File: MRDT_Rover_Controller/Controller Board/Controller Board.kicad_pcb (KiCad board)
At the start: 2 copper layers, 137.6 x 81.5 mm, 32 parts, among them Q1 S8050, SW1 EG1218

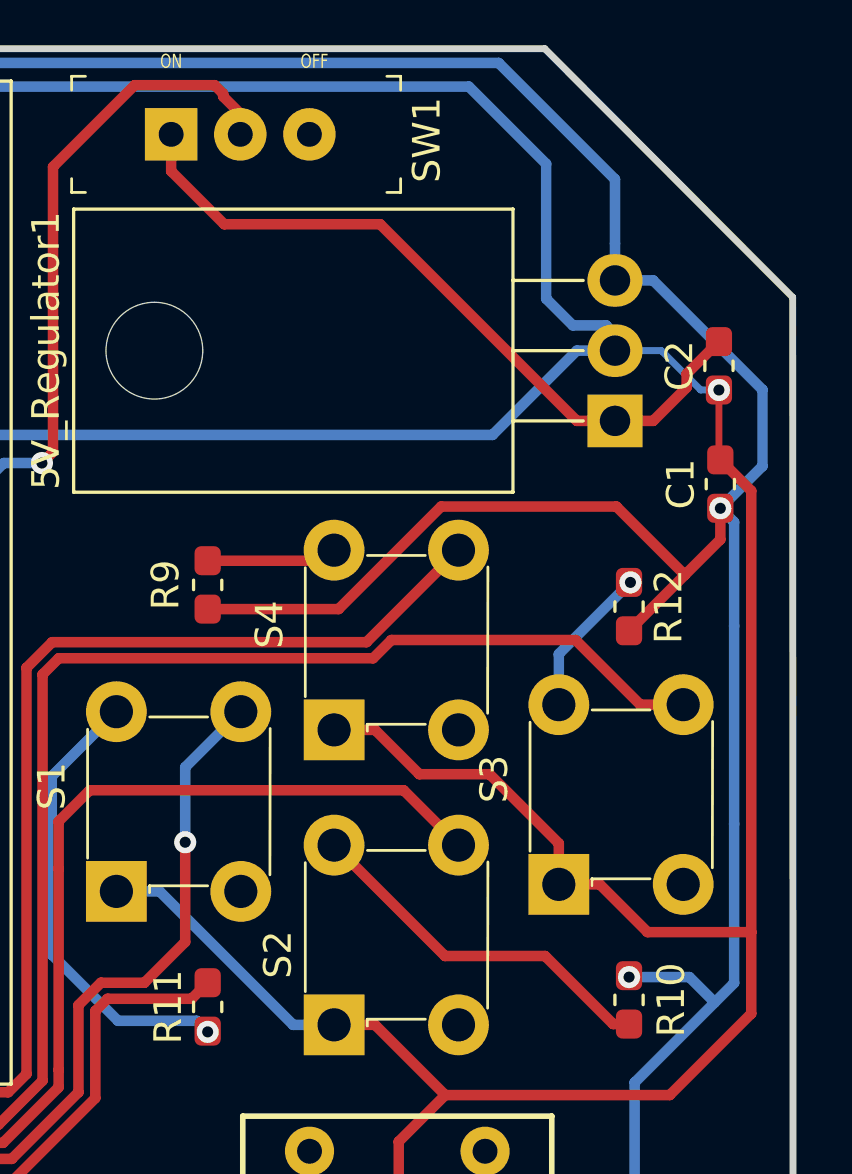
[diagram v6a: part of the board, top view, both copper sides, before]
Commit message: Trace corners re-adjusted
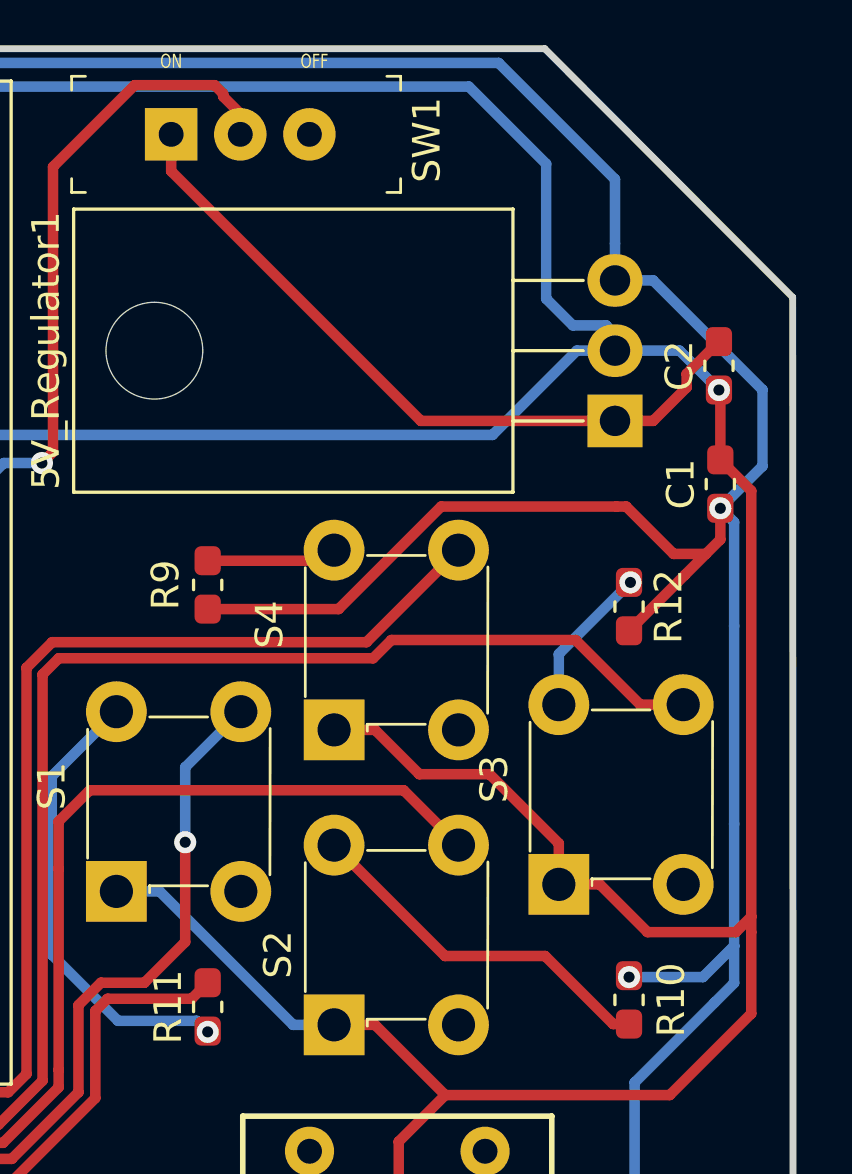
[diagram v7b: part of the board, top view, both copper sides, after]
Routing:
- net 5V: track 419.7 -> 421.0 mm
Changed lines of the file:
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@@
     (thickness 1.6)
     (drawings 30)
-    (tracks 651)
+    (tracks 655)
     (zones 0)
     (modules 32)
@@
   )
   (setup
-    (last_trace_width 0.25)
+    (last_trace_width 0.381)
     (user_trace_width 0.381)
     (user_trace_width 15)
@@
   (segment (start 92.71 96.278765) (end 86.995 90.563765) (width 0.381) (layer F.Cu) (net 14))
   (segment (start 92.71 97.536) (end 92.71 96.278765) (width 0.381) (layer F.Cu) (net 14))
-  (segment (start 210.82 64.4652) (end 210.7692 64.4144) (width 0.381) (layer F.Cu) (net 14))
   (segment (start 210.7692 66.8922) (end 210.82 66.943) (width 0.25) (layer F.Cu) (net 14))
-  (segment (start 210.7692 64.4144) (end 210.7692 66.8922) (width 0.25) (layer F.Cu) (net 14))
   (segment (start 210.7692 64.4144) (end 210.7692 64.4144) (width 0.381) (layer F.Cu) (net 14))
   (via (at 210.7692 64.4144) (size 0.8) (drill 0.4) (layers F.Cu B.Cu) (net 14))
-  (segment (start 210.7692 64.4144) (end 210.1088 64.4144) (width 0.25) (layer B.Cu) (net 14))
-  (segment (start 208.6864 62.992) (end 207.01 62.992) (width 0.25) (layer B.Cu) (net 14))
-  (segment (start 210.1088 64.4144) (end 208.6864 62.992) (width 0.25) (layer B.Cu) (net 14))
   (segment (start 189.527 82.55) (end 188.976 82.55) (width 0.381) (layer B.Cu) (net 14))
   (segment (start 200.871 89.916) (end 198.331 87.376) (width 0.381) (layer F.Cu) (net 14))
@@
   (segment (start 206.459 82.296) (end 204.978 82.296) (width 0.381) (layer F.Cu) (net 14))
   (segment (start 208.1862 84.0232) (end 206.459 82.296) (width 0.381) (layer F.Cu) (net 14))
-  (segment (start 211.9376 84.0232) (end 208.1862 84.0232) (width 0.381) (layer F.Cu) (net 14))
   (segment (start 211.9376 84.0232) (end 211.9376 86.9696) (width 0.381) (layer F.Cu) (net 14))
-  (segment (start 211.9376 68.0606) (end 211.9376 84.0232) (width 0.381) (layer F.Cu) (net 14))
   (segment (start 198.331 76.708) (end 196.85 76.708) (width 0.381) (layer F.Cu) (net 14))
   (segment (start 199.934391 78.311391) (end 198.331 76.708) (width 0.381) (layer F.Cu) (net 14))
@@
   (segment (start 196.85 87.376) (end 195.369 87.376) (width 0.381) (layer B.Cu) (net 14))
   (segment (start 195.369 87.376) (end 190.543 82.55) (width 0.381) (layer B.Cu) (net 14))
-  (segment (start 205.629 65.532) (end 198.517 58.42) (width 0.381) (layer F.Cu) (net 15))
-  (segment (start 207.01 65.532) (end 205.629 65.532) (width 0.381) (layer F.Cu) (net 15))
-  (segment (start 190.9572 56.4998) (end 190.9572 55.1688) (width 0.381) (layer F.Cu) (net 15))
-  (segment (start 192.8774 58.42) (end 190.9572 56.4998) (width 0.381) (layer F.Cu) (net 15))
-  (segment (start 198.517 58.42) (end 192.8774 58.42) (width 0.381) (layer F.Cu) (net 15))
+  (segment (start 211.3788 84.0232) (end 211.9376 83.4644) (width 0.381) (layer F.Cu) (net 14))
+  (segment (start 208.1862 84.0232) (end 211.3788 84.0232) (width 0.381) (layer F.Cu) (net 14))
+  (segment (start 211.9376 68.0606) (end 211.9376 83.4644) (width 0.381) (layer F.Cu) (net 14))
+  (segment (start 211.9376 83.4644) (end 211.9376 84.0232) (width 0.381) (layer F.Cu) (net 14))
+  (segment (start 210.82 64.4652) (end 210.7692 64.4144) (width 0.381) (layer F.Cu) (net 14))
+  (segment (start 210.82 66.943) (end 210.82 64.4652) (width 0.381) (layer F.Cu) (net 14))
+  (segment (start 209.3468 62.992) (end 207.01 62.992) (width 0.381) (layer B.Cu) (net 14))
+  (segment (start 210.7692 64.4144) (end 209.3468 62.992) (width 0.381) (layer B.Cu) (net 14))
   (segment (start 190.743669 54.65329) (end 190.592679 54.80428) (width 0.25) (layer F.Cu) (net 15))
   (segment (start 191.170731 54.65329) (end 190.743669 54.65329) (width 0.25) (layer F.Cu) (net 15))
@@
   (segment (start 209.6008 63.8328) (end 210.7692 62.6644) (width 0.381) (layer F.Cu) (net 15))
   (segment (start 209.6008 64.3222) (end 209.6008 63.8328) (width 0.381) (layer F.Cu) (net 15))
+  (segment (start 190.9572 56.4998) (end 190.9572 55.1688) (width 0.381) (layer F.Cu) (net 15))
+  (segment (start 199.9894 65.532) (end 190.9572 56.4998) (width 0.381) (layer F.Cu) (net 15))
+  (segment (start 207.01 65.532) (end 199.9894 65.532) (width 0.381) (layer F.Cu) (net 15))
   (segment (start 167.132 109.2708) (end 163.2204 113.1824) (width 0.381) (layer F.Cu) (net 22))
   (segment (start 163.2204 113.1824) (end 163.2204 116.9416) (width 0.381) (layer F.Cu) (net 22))
@@
   (via (at 210.82 68.693) (size 0.8) (drill 0.4) (layers F.Cu B.Cu) (net 56))
   (segment (start 210.82 68.693) (end 211.319072 69.192072) (width 0.381) (layer B.Cu) (net 56))
-  (segment (start 211.319072 80.102672) (end 211.319072 85.860928) (width 0.381) (layer B.Cu) (net 56))
   (segment (start 211.319072 69.192072) (end 211.319072 72.939872) (width 0.381) (layer B.Cu) (net 56))
   (segment (start 211.319072 72.939872) (end 211.319072 80.102672) (width 0.381) (layer B.Cu) (net 56))
@@
   (segment (start 209.3468 101.6) (end 209.3468 95.751115) (width 0.381) (layer B.Cu) (net 56))
   (segment (start 210.82 69.822) (end 210.82 68.693) (width 0.381) (layer F.Cu) (net 56))
-  (segment (start 209.7024 85.6488) (end 210.6168 86.5632) (width 0.381) (layer B.Cu) (net 56))
-  (segment (start 207.518 85.6488) (end 209.7024 85.6488) (width 0.381) (layer B.Cu) (net 56))
   (segment (start 211.319072 85.860928) (end 210.6168 86.5632) (width 0.381) (layer B.Cu) (net 56))
   (segment (start 210.6168 86.5632) (end 207.7212 89.4588) (width 0.381) (layer B.Cu) (net 56))
@@
   (segment (start 185.0644 94.1718) (end 185.0644 93.176072) (width 0.381) (layer F.Cu) (net 56))
   (segment (start 185.0644 93.176072) (end 188.214 90.026472) (width 0.381) (layer F.Cu) (net 56))
-  (segment (start 207.0608 68.6308) (end 209.536 71.106) (width 0.381) (layer F.Cu) (net 56))
   (segment (start 192.278 72.3392) (end 197.012858 72.3392) (width 0.381) (layer F.Cu) (net 56))
   (segment (start 200.721258 68.6308) (end 207.0608 68.6308) (width 0.381) (layer F.Cu) (net 56))
   (segment (start 197.012858 72.3392) (end 200.721258 68.6308) (width 0.381) (layer F.Cu) (net 56))
   (segment (start 207.518 73.124) (end 209.536 71.106) (width 0.381) (layer F.Cu) (net 56))
-  (segment (start 209.536 71.106) (end 210.82 69.822) (width 0.381) (layer F.Cu) (net 56))
+  (segment (start 207.0608 68.6308) (end 207.1116 68.6308) (width 0.25) (layer F.Cu) (net 56))
+  (segment (start 207.0608 68.6308) (end 207.4164 68.6308) (width 0.381) (layer F.Cu) (net 56))
+  (segment (start 209.1296 70.344) (end 210.298 70.344) (width 0.381) (layer F.Cu) (net 56))
+  (segment (start 207.4164 68.6308) (end 209.1296 70.344) (width 0.381) (layer F.Cu) (net 56))
+  (segment (start 209.536 71.106) (end 210.298 70.344) (width 0.381) (layer F.Cu) (net 56))
+  (segment (start 210.298 70.344) (end 210.82 69.822) (width 0.381) (layer F.Cu) (net 56))
+  (segment (start 210.192544 85.6488) (end 211.319072 84.522272) (width 0.381) (layer B.Cu) (net 56))
+  (segment (start 207.518 85.6488) (end 210.192544 85.6488) (width 0.381) (layer B.Cu) (net 56))
+  (segment (start 211.319072 80.102672) (end 211.319072 84.522272) (width 0.381) (layer B.Cu) (net 56))
+  (segment (start 211.319072 84.522272) (end 211.319072 85.860928) (width 0.381) (layer B.Cu) (net 56))
   (segment (start 170.086 81.874) (end 184.904 67.056) (width 0.381) (layer B.Cu) (net 57))
   (segment (start 168.83 81.874) (end 170.086 81.874) (width 0.381) (layer B.Cu) (net 57))

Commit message: Silkscreen Updated
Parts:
- moved G*** 0.07 mm to (92.7, 127.4)
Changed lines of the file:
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@@
   )
   (setup
-    (last_trace_width 0.381)
+    (last_trace_width 0.25)
     (user_trace_width 0.381)
     (user_trace_width 15)
@@
   )
   (module MRDT_Silkscreens:0_MRDT_Logo_10mm (layer F.Cu)
-    (at 92.6084 127.4572)
+    (at 92.6592 127.4064)
     (tags "Logo, MRDT")
     (fp_text reference G*** (at -1.143 6.4008) (layer Dwgs.User) hide
